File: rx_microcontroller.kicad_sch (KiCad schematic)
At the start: 11 parts, among them U2 NRF54L15-QFAA-R

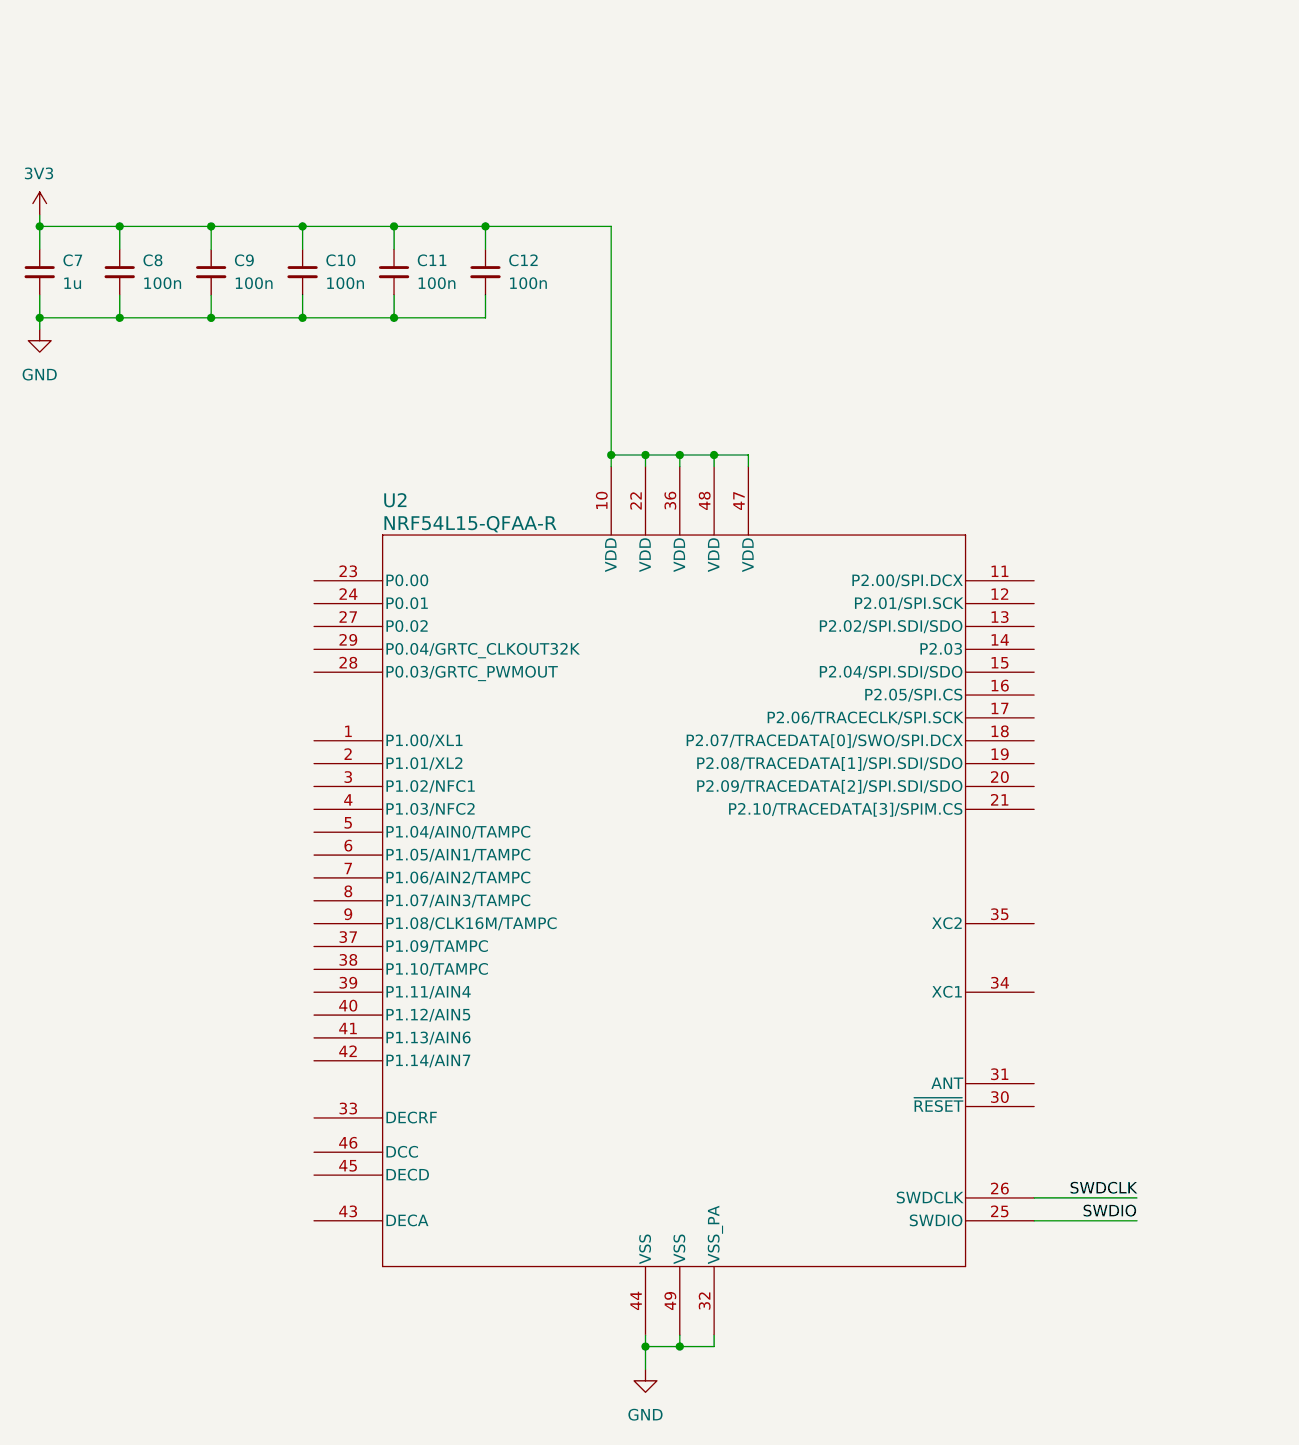
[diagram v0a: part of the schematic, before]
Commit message: Added USB to UART circuitry, cleaned up top sheets, added more supporting circuitry for TX MCU
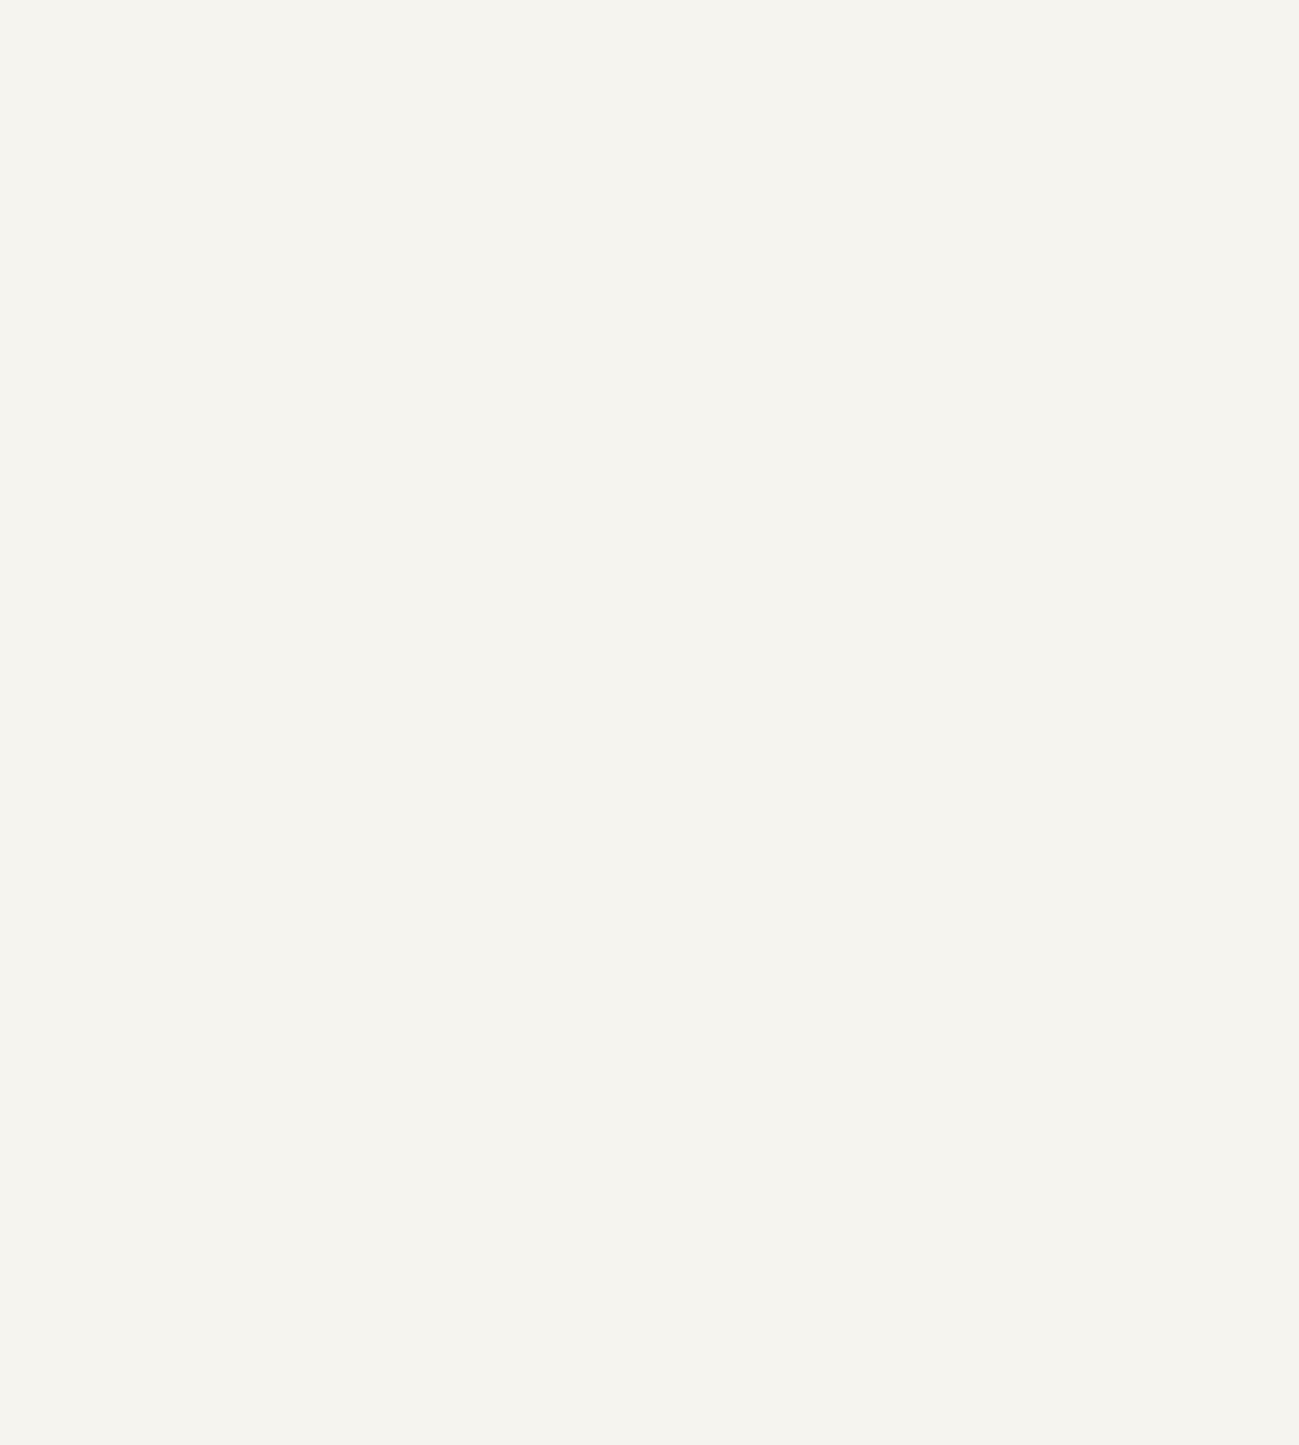
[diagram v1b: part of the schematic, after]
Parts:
- removed C10, C11, C12, C8, C9: 100n, symbol Device:C_Small
- removed C7: 1u, symbol Device:C_Small
- removed U2: NRF54L15-QFAA-R, Team_512_MCUs:NRF54L15-QFAA-R, symbol Team_512_MCUs:NRF54L15-QFAA-R

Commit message: Finished schematic, added power section for external power (both power supply and battery), added current sensing for TX microcontroller
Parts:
- removed TP5, TP6, TP7, TP8: 1.0mm, TestPoint:TestPoint_Pad_D1.0mm, symbol Connector:TestPoint
- added C17, C21, C22: 2.2u, Capacitor_SMD:C_0603_1608Metric_Pad1.08x0.95mm_HandSolder, symbol AERO_Capacitors:C_0603
- added C18: 10u, symbol Device:C_Small
- added C19, C26, C27, C30: 100n, symbol Device:C_Small
- added C20: 10n, Capacitor_SMD:C_0603_1608Metric_Pad1.08x0.95mm_HandSolder, symbol AERO_Capacitors:C_0603
- added C23, C29: 8p, Capacitor_SMD:C_0201_0603Metric, symbol Device:C_Small
- added C24: 3.9p, Capacitor_SMD:C_0603_1608Metric_Pad1.08x0.95mm_HandSolder, symbol AERO_Capacitors:C_0603
- added C25: 1.5p, Capacitor_SMD:C_0201_0603Metric, symbol Device:C_Small
- added C28: 2.0p, Capacitor_SMD:C_0201_0603Metric, symbol Device:C_Small
- added C31: 0.3p, Capacitor_SMD:C_0201_0603Metric, symbol Device:C_Small
- added L5: 4.7u, Inductor_SMD:L_0603_1608Metric_Pad1.05x0.95mm_HandSolder, symbol Device:L_Small
- added L6: 2.7n, Inductor_SMD:L_0201_0603Metric, symbol Device:L_Small
- added L7, L8: 3.5n, Inductor_SMD:L_0201_0603Metric, symbol Device:L_Small
- added R13, R15, R16: 0, Resistor_SMD:R_0603_1608Metric_Pad0.98x0.95mm_HandSolder, symbol AERO_Resistors:R_0603
- added R14: 1k, Resistor_SMD:R_0603_1608Metric_Pad0.98x0.95mm_HandSolder, symbol AERO_Resistors:R_0603
- added SW2: KMR211G LFS, Button_Switch_SMD:SW_Push_1P1T_NO_CK_KMR2, symbol Switch:SW_Push
- added TP10, TP11, TP12, TP13, TP14, TP15, TP16, TP17, TP18: 1.0mm, TestPoint:TestPoint_Pad_D1.0mm, symbol Connector:TestPoint
- added U4: nRF54L15-QFAA-R, Team_512_MCUs:NRF54L15-QFAA-R, symbol Team_512_MCUs:NRF54L15-QFAA-R
- added Y2: ECS-320-CDX-2374, Team_512_Oscillators:ECS-320-CDX-2374, symbol Team_512_Oscillators:ECS-320-CDX-2374
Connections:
- net +3.3V: now also TP15.1
- net GND: now also C17.2, C18.2, C19.2, C20.2, C21.2, C22.2, C23.2, C24.2, C25.2, C26.2, C27.2, C28.2, C29.2, C30.2, C31.2, SW2.1, TP18.1, U4.32 (VSS_PA), U4.44 (VSS), U4.49 (VSS), Y2.2 (GND), Y2.4 (GND)
- net SWDCLK: now also TP16.1, U4.26 (SWDCLK)
- net SWDIO: now also TP17.1, U4.25 (SWDIO)
- new net: R15.2, U4.5 (P1.04/AIN0/TAMPC)
- new net: R16.2, U4.8 (P1.07/AIN3/TAMPC)
- new net: C28.1, L7.2, L8.1
- new net: C22.1, L5.1, R13.2, TP10.1, U4.45 (DECD)
- new net: L5.2, TP11.1, U4.46 (DCC)
- new net: C25.1, L6.2, L7.1
- new net: C23.1, U4.35 (XC2), Y2.1
- new net: C29.1, U4.34 (XC1), Y2.3
- new net: L6.1, U4.31 (ANT)
- new net: C17.1, C20.1, C21.1, R13.1, TP12.1, U4.33 (DECRF), U4.43 (DECA)
- new net 3V3: C18.1, C19.1, C26.1, C27.1, C30.1, TP13.1, U4.10 (VDD), U4.22 (VDD), U4.36 (VDD), U4.47 (VDD), U4.48 (VDD)
- new net BOOT_B: U4.24 (P0.01)
- new net PWM+: R15.1, U4.6 (P1.05/AIN1/TAMPC)
- new net PWM-: R16.1, U4.7 (P1.06/AIN2/TAMPC)
- new net RF: C31.1, L8.2
- new net nRF_URXD_B: U4.11 (P2.00/SPI.DCX)
- new net nRF_UTXD_B: U4.13 (P2.02/SPI.SDI/SDO)
- new net nRF_~{RESET}_B: R14.2, SW2.2
- new net ~{RESET}: C24.1, R14.1, TP14.1, U4.30 (~{RESET})
- no-connect marks 0 -> 24
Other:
- note added: "ADD OSCILLATOR"
- note added: "Change to header?"
- note added: "Replace w/ FB if needed"
- note added: "SEE DATASHEET FOR GND ROUTING"
- note added: "~{RESET} pulled up internally"

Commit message: Made most capacitors 0402 for mcu sheets, defined board shape and started layout
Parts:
- removed C17, C21, C22: 2.2u, Capacitor_SMD:C_0603_1608Metric_Pad1.08x0.95mm_HandSolder, symbol AERO_Capacitors:C_0603
- removed C18: 10u, symbol Device:C_Small
- removed C19, C26, C27, C30: 100n, symbol Device:C_Small
- removed C20: 10n, Capacitor_SMD:C_0603_1608Metric_Pad1.08x0.95mm_HandSolder, symbol AERO_Capacitors:C_0603
- removed C24: 3.9p, Capacitor_SMD:C_0603_1608Metric_Pad1.08x0.95mm_HandSolder, symbol AERO_Capacitors:C_0603
- removed R13: 0, Resistor_SMD:R_0603_1608Metric_Pad0.98x0.95mm_HandSolder, symbol AERO_Resistors:R_0603
- added C19, C24: 2.2u, Capacitor_SMD:C_0402_1005Metric_Pad0.74x0.62mm_HandSolder, symbol AERO_Capacitors:C_0402
- added C20: 10u, Capacitor_SMD:C_0402_1005Metric_Pad0.74x0.62mm_HandSolder, symbol AERO_Capacitors:C_0402
- added C21, C28, C29, C32: 100n, Capacitor_SMD:C_0402_1005Metric_Pad0.74x0.62mm_HandSolder, symbol AERO_Capacitors:C_0402
- added C22: 10n, Capacitor_SMD:C_0402_1005Metric_Pad0.74x0.62mm_HandSolder, symbol AERO_Capacitors:C_0402
- added C23: 2.2n, Capacitor_SMD:C_0402_1005Metric_Pad0.74x0.62mm_HandSolder, symbol AERO_Capacitors:C_0402
- added C26: 3.9p, Capacitor_SMD:C_0402_1005Metric_Pad0.74x0.62mm_HandSolder, symbol AERO_Capacitors:C_0402
- added R14: 0, Resistor_SMD:R_0402_1005Metric_Pad0.72x0.64mm_HandSolder, symbol AERO_Resistors:R_0402
- renumbered C23 to C25, C25 to C27, C28 to C30, C29 to C31, C31 to C33, R14 to R15, R15 to R16, R16 to R17, TP10 to TP12, TP11 to TP13, TP12 to TP14, TP13 to TP15, TP14 to TP16, TP15 to TP17, TP16 to TP18, TP17 to TP19, TP18 to TP20, U4 to U2
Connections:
- net 3V3: now also C20.1, C21.1, C28.1, C29.1, C32.1
- net GND: now also C19.2, C20.2, C21.2, C22.2, C23.2, C24.2, C26.2, C28.2, C29.2, C32.2
- net ~{RESET}: now also C26.1
- net at L5.1, TP12.1, U2.45 (DECD): now also C24.1, R14.1
- net at TP14.1, U2.33 (DECRF), U2.43 (DECA): now also C19.1, C22.1, C23.1, R14.2
